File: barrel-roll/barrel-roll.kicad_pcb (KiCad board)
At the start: 2 copper layers, 46.7 x 53 mm, 16 parts, among them M1 Motor_DC, M2 Motor_DC, U1 XIAO-RP2040-DIP, U2 DRV8833PW, U3 WeaponMotor, U4 Recever

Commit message: Added esp32 support, and worked on the battery conenctor.
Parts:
- removed TP1: BatteryPower, Connector_Wire:SolderWire-2sqmm_1x01_D2mm_OD3.9mm
- removed TP2: BattteryGND, Connector_Wire:SolderWire-2sqmm_1x01_D2mm_OD3.9mm
- added XT1: ~, Connector_AMASS:AMASS_XT30UPB-F_1x02_P5.0mm_Vertical, F.Cu at (136.7, 63.5)
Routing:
- net Net-(XT1-Power): track 32.9 -> 13.0 mm
- net GND: track 132.3 -> 139.6 mm

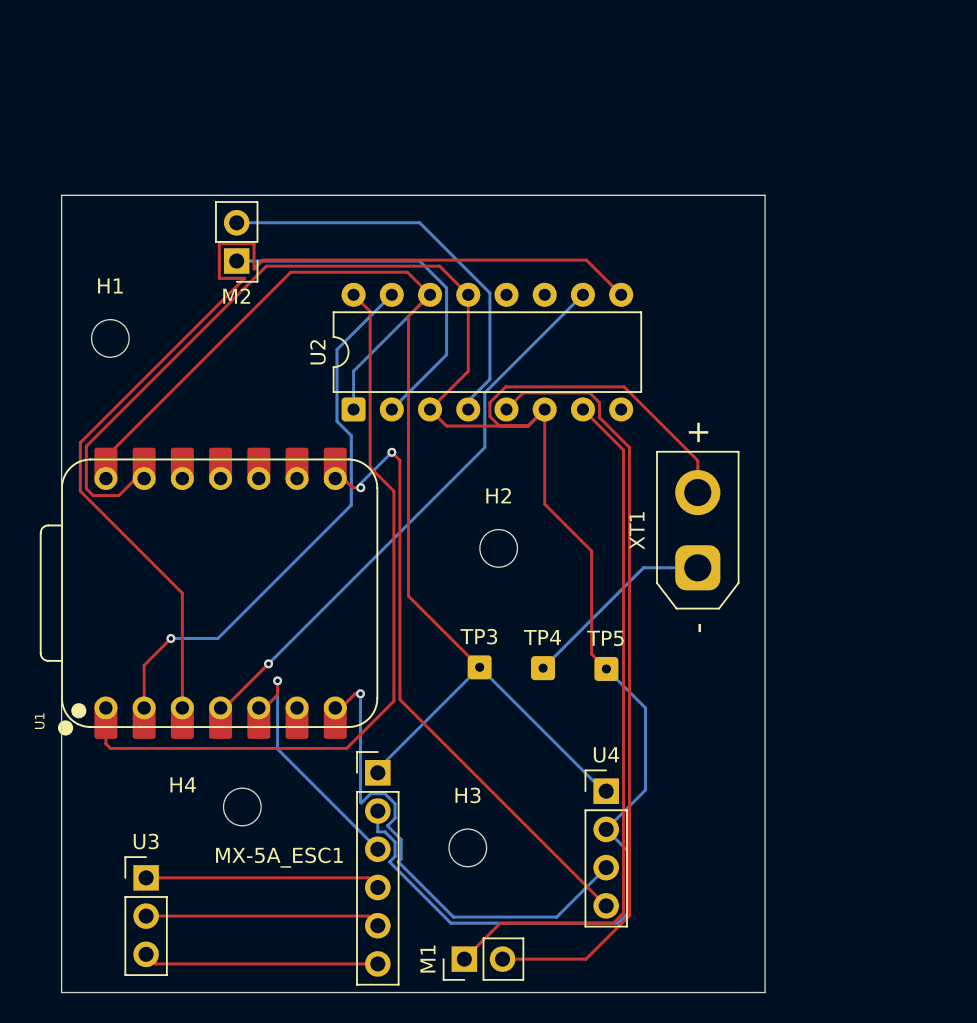
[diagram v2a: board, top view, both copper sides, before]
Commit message: Updated the pcb and the models.
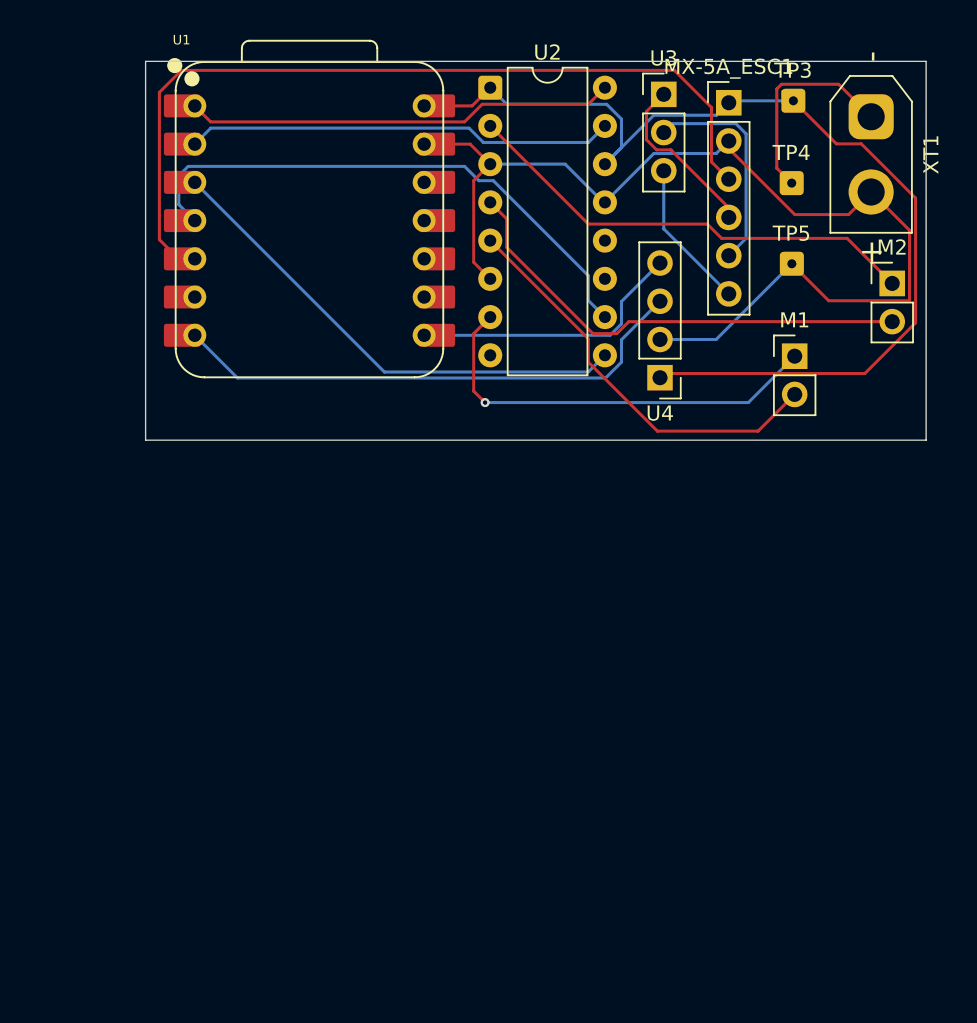
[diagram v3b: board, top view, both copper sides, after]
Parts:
- removed H1, H2, H3, H4: MountingHole, MountingHole:MountingHole_2.5mm
- moved U3 62.4 mm to (134.5, 32.1)
- moved MX-5A_ESC1 50.3 mm to (138.8, 32.6)
- moved M1 45.7 mm to (143.2, 49.5), turned to 0 degrees
- moved M2 43.6 mm to (149.6, 44.6), turned to 0 degrees
- moved TP3 43.0 mm to (143.1, 32.5)
- moved TP4 36.2 mm to (143.0, 38.0)
- moved XT1 32.1 mm to (148.2, 33.5), turned to -90 degrees
- moved TP5 29.6 mm to (143.0, 43.3)
- moved U4 27.7 mm to (134.2, 50.9), turned to 180 degrees
- moved U1 25.5 mm to (110.9, 40.5), turned to 0 degrees
- moved U2 23.2 mm to (122.9, 31.6), turned to 0 degrees
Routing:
- net GND: track 139.6 -> 72.4 mm
- net Net-(MX-5A_ESC1-SIG): track 16.6 -> 56.2 mm, vias 1 -> 0
- net BIN1: track 69.8 -> 32.9 mm
- net BOUT2: track 51.4 -> 27.4 mm
- net Net-(U1-GPIO1/RX): track 41.3 -> 18.5 mm, vias 2 -> 0
- net AIN1: track 50.7 -> 28.6 mm
- net BOUT1: track 46.4 -> 28.3 mm, vias 0 -> 1
- net BT1P: track 86.8 -> 71.5 mm
- net AIN2: track 37.4 -> 28.5 mm, vias 1 -> 0
- net AOUT1: track 24.3 -> 31.0 mm
- net Net-(MX-5A_ESC1-M3): track 15.7 -> 9.97 mm
- net AOUT2: track 27.1 -> 31.8 mm
- net Net-(MX-5A_ESC1-M1): track 15.7 -> 11.5 mm
- net Net-(U1-GPIO0/TX): track 33.6 -> 35.1 mm, vias 1 -> 0
- net Net-(MX-5A_ESC1-M2): track 15.7 -> 14.6 mm
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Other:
- board size 46.7 x 53 mm -> 51.9 x 25.2 mm

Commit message: Added pcb design elements.
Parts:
- added G***: LOGO, Graphics:WeaponSmall, F.Cu at (100.4, 49.8)
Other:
- board text added: "150g combat robot"
- board text added: "Barrel Roll"
